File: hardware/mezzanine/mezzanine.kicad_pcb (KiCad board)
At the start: 2 copper layers, 85 x 56 mm, 43 parts, among them J1 USB_A, J2 USB_C, J3 HDMI_D, J4 HDMI_D, U1 AP22653W6, U2 TPD4EUSB30, U3 TPD4EUSB30, U4 TPD4EUSB30, U5 MagJack-A70-112-331N126, U6 RT9742SNGV, U7 74LVC1G07SE-7

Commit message: finished mezzanine signal routing
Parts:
- removed C10, C11, C12, C13, C14: 100n, Capacitor_SMD:C_0402_1005Metric
- removed the C7 at (263.2, 80.6)
- removed the C8 at (257.2, 86.8)
- removed the C9 at (248.0, 97.2)
- removed H4: MountingHole, MountingHole:MountingHole_2.7mm_M2.5
- removed TP1: TestPoint, TestPoint:TestPoint_Pad_2.0x2.0mm
- added H3: MountingHole, MountingHole:MountingHole_2.7mm_M2.5, F.Cu at (81.5, 23.5)
- C7: renamed from C15; footprint Capacitor_SMD:C_0402_1005Metric -> Capacitor_SMD:C_0603_1608Metric
- C8: renamed from C16; footprint Capacitor_SMD:C_0402_1005Metric -> Capacitor_SMD:C_0603_1608Metric
- C9: renamed from C17; footprint Capacitor_SMD:C_0402_1005Metric -> Capacitor_SMD:C_0603_1608Metric
- Module1: value cm4-module-A -> hirose-100
- Module2: value cm4-module-B -> hirose-100
- R1: footprint Resistor_SMD:R_0402_1005Metric -> Resistor_SMD:R_0805_2012Metric
- R4, R5, R6: footprint Resistor_SMD:R_0402_1005Metric -> Resistor_SMD:R_0603_1608Metric
- U2, U4: moved to B.Cu
- moved R2 200.5 mm to (40.0, 69.5), turned to -90 degrees
- moved R3 198.5 mm to (38.0, 69.5), turned to -90 degrees
- moved C1 178.4 mm to (90.5, 56.0), turned to 180 degrees
- moved C3 170.1 mm to (94.0, 59.5), turned to 90 degrees
- moved C8 166.4 mm to (39.0, 73.5)
- moved C9 166.3 mm to (39.0, 72.0), turned to 180 degrees
- moved R6 165.7 mm to (23.0, 67.0), turned to 90 degrees
- moved D2 164.6 mm to (21.0, 63.0), turned to 90 degrees
- moved U1 164.3 mm to (90.5, 59.5), turned to -90 degrees
- moved R1 163.3 mm to (90.5, 63.0)
- moved R7 162.7 mm to (23.0, 63.0), turned to 90 degrees
- moved U2 161.9 mm to (89.0, 64.0)
- moved D1 160.3 mm to (21.0, 67.0), turned to 90 degrees
- moved U7 159.9 mm to (22.0, 59.0), turned to -90 degrees
- moved C5 159.3 mm to (96.0, 59.5), turned to 90 degrees
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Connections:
- net /usb/nOCS1 renamed /usb/nUSB_CURR_FAULT
- J3 pad 1: /HDMI1_HOTPLUG -> /HDMI0_HOTPLUG
- J3 pad 11: /HDMI1_TX0_N -> /HDMI0_TX0_N
- J3 pad 12: /HDMI1_CLK_P -> /HDMI0_CLK_P
- J3 pad 14: /HDMI1_CLK_N -> /HDMI0_CLK_N
- J3 pad 15: /HDMI1_CEC -> /HDMI0_CEC
- J3 pad 17: /HDMI1_SCL -> /HDMI0_SCL
- J3 pad 18: /HDMI1_SDA -> /HDMI0_SDA
- J3 pad 3: /HDMI1_TX2_P -> /HDMI0_TX2_P
- J3 pad 5: /HDMI1_TX2_N -> /HDMI0_TX2_N
- J3 pad 6: /HDMI1_TX1_P -> /HDMI0_TX1_P
- J3 pad 8: /HDMI1_TX1_N -> /HDMI0_TX1_N
- J3 pad 9: /HDMI1_TX0_P -> /HDMI0_TX0_P
- J4 pad 1: /HDMI0_HOTPLUG -> /HDMI1_HOTPLUG
- J4 pad 11: /HDMI0_TX0_N -> /HDMI1_TX0_N
- J4 pad 12: /HDMI0_CLK_P -> /HDMI1_CLK_P
- J4 pad 14: /HDMI0_CLK_N -> /HDMI1_CLK_N
- J4 pad 15: /HDMI0_CEC -> /HDMI1_CEC
- J4 pad 17: /HDMI0_SCL -> /HDMI1_SCL
- J4 pad 18: /HDMI0_SDA -> /HDMI1_SDA
- J4 pad 3: /HDMI0_TX2_P -> /HDMI1_TX2_P
- J4 pad 5: /HDMI0_TX2_N -> /HDMI1_TX2_N
- J4 pad 6: /HDMI0_TX1_P -> /HDMI1_TX1_P
- J4 pad 8: /HDMI0_TX1_N -> /HDMI1_TX1_N
- J4 pad 9: /HDMI0_TX0_P -> /HDMI1_TX0_P
- Module1 pad 10: /TRD0_N -> /TRD3_P
- Module1 pad 100: unconnected-(Module1-Pad100) -> GND
- Module1 pad 11: /TRD2_P -> /TRD1_N
- Module1 pad 12: /TRD0_P -> /TRD3_N
- Module1 pad 15: /ETH_LEDY -> /TR1_TAP
- Module1 pad 16: unconnected-(Module1-Pad16) -> /TR3_TAP
- Module1 pad 17: /ETH_LEDG -> /TR1_TAP
- Module1 pad 18: unconnected-(Module1-Pad18) -> /TR3_TAP
- Module1 pad 19: unconnected-(Module1-Pad19) -> /TR1_TAP
- Module1 pad 20: unconnected-(Module1-Pad20) -> /TR3_TAP
- Module1 pad 21: /nPI_LED_ACTIVITY -> GND
- Module1 pad 23: GND -> /TR2_TAP
- Module1 pad 24: unconnected-(Module1-Pad24) -> /TR0_TAP
- Module1 pad 25: unconnected-(Module1-Pad25) -> /TR2_TAP
- Module1 pad 27: /TR1_TAP -> /TR2_TAP
- Module1 pad 29: /TR1_TAP -> GND
- Module1 pad 3: /TRD3_P -> /TRD0_N
- Module1 pad 30: /TR0_TAP -> GND
- Module1 pad 31: /TR1_TAP -> VBUS
- Module1 pad 32: GND -> VBUS
- Module1 pad 33: GND -> VBUS
- Module1 pad 34: unconnected-(Module1-Pad34) -> VBUS
- Module1 pad 35: unconnected-(Module1-Pad35) -> VBUS
- Module1 pad 36: /TR2_TAP -> VBUS
- Module1 pad 37: /TR3_TAP -> VBUS
- Module1 pad 38: /TR2_TAP -> VBUS
- Module1 pad 39: /TR3_TAP -> VBUS
- Module1 pad 4: /TRD1_P -> /TRD2_P
- Module1 pad 40: /TR2_TAP -> VBUS
- Module1 pad 41: /TR3_TAP -> VBUS
- Module1 pad 42: GND -> VBUS
- Module1 pad 43: GND -> VBUS
- Module1 pad 44: unconnected-(Module1-Pad44) -> VBUS
- Module1 pad 45: unconnected-(Module1-Pad45) -> GND
- Module1 pad 46: unconnected-(Module1-Pad46) -> GND
- Module1 pad 47: unconnected-(Module1-Pad47) -> GND
- Module1 pad 48: unconnected-(Module1-Pad48) -> /+3.3v
- Module1 pad 49: unconnected-(Module1-Pad49) -> /AnalogIP1
- Module1 pad 5: /TRD3_N -> /TRD0_P
- Module1 pad 50: unconnected-(Module1-Pad50) -> /+3.3v
- Module1 pad 51: unconnected-(Module1-Pad51) -> /AnalogIP0
- Module1 pad 54: unconnected-(Module1-Pad54) -> /ETH_LEDY
- Module1 pad 55: unconnected-(Module1-Pad55) -> /USB2_HOST_P
- Module1 pad 56: unconnected-(Module1-Pad56) -> /ETH_LEDG
- Module1 pad 57: unconnected-(Module1-Pad57) -> /USB2_HOST_N
- Module1 pad 58: unconnected-(Module1-Pad58) -> /nPI_LED_ACTIVITY
- Module1 pad 6: /TRD1_N -> /TRD2_N
- Module1 pad 60: GND -> /nPI_LED_PWR
- Module1 pad 61: unconnected-(Module1-Pad61) -> /USB2_DEV_N
- Module1 pad 62: unconnected-(Module1-Pad62) -> GND
- Module1 pad 63: unconnected-(Module1-Pad63) -> /USB2_DEV_P
- Module1 pad 64: unconnected-(Module1-Pad64) -> GND
- Module1 pad 67: unconnected-(Module1-Pad67) -> /HDMI1_HOTPLUG
- Module1 pad 68: unconnected-(Module1-Pad68) -> /HDMI0_HOTPLUG
- Module1 pad 69: unconnected-(Module1-Pad69) -> /HDMI1_CEC
- Module1 pad 70: unconnected-(Module1-Pad70) -> /HDMI0_CEC
- Module1 pad 71: GND -> /HDMI1_SDA
- Module1 pad 72: unconnected-(Module1-Pad72) -> /HDMI0_SDA
- Module1 pad 73: unconnected-(Module1-Pad73) -> /HDMI1_SCL
- Module1 pad 74: GND -> /HDMI0_SCL
- Module1 pad 75: unconnected-(Module1-Pad75) -> GND
- Module1 pad 76: unconnected-(Module1-Pad76) -> GND
- Module1 pad 77: VBUS -> /HDMI1_TX0_P
- Module1 pad 78: unconnected-(Module1-Pad78) -> /HDMI0_TX0_N
- Module1 pad 79: VBUS -> /HDMI1_TX0_N
- Module1 pad 80: unconnected-(Module1-Pad80) -> /HDMI0_TX0_P
- Module1 pad 81: VBUS -> GND
- Module1 pad 82: unconnected-(Module1-Pad82) -> GND
- Module1 pad 83: VBUS -> /HDMI1_TX2_P
- Module1 pad 84: /+3.3v -> /HDMI0_TX2_N
- Module1 pad 85: VBUS -> /HDMI1_TX2_N
- Module1 pad 86: /+3.3v -> /HDMI0_TX2_P
- Module1 pad 87: VBUS -> GND
- Module1 pad 88: unconnected-(Module1-Pad88) -> GND
- Module1 pad 89: unconnected-(Module1-Pad89) -> /HDMI0_TX1_P
- Module1 pad 9: /TRD2_N -> /TRD1_P
- Module1 pad 90: unconnected-(Module1-Pad90) -> /HDMI1_CLK_N
- Module1 pad 91: unconnected-(Module1-Pad91) -> /HDMI0_TX1_N
- Module1 pad 92: unconnected-(Module1-Pad92) -> /HDMI1_CLK_P
- Module1 pad 93: unconnected-(Module1-Pad93) -> GND
- Module1 pad 94: /AnalogIP1 -> GND
- Module1 pad 95: /nPI_LED_PWR -> /HDMI0_CLK_P
- Module1 pad 96: /AnalogIP0 -> /HDMI1_TX1_N
- Module1 pad 97: unconnected-(Module1-Pad97) -> /HDMI0_CLK_N
- Module1 pad 98: GND -> /HDMI1_TX1_P
- Module1 pad 99: unconnected-(Module1-Pad99) -> GND
- Module2 pad 100: /HDMI0_SCL -> unconnected-(Module2-Pad100)
- Module2 pad 13: GND -> unconnected-(Module2-Pad13)
- Module2 pad 14: GND -> unconnected-(Module2-Pad14)
- Module2 pad 19: GND -> unconnected-(Module2-Pad19)
- Module2 pad 20: GND -> unconnected-(Module2-Pad20)
- Module2 pad 25: GND -> unconnected-(Module2-Pad25)
- Module2 pad 26: GND -> unconnected-(Module2-Pad26)
- Module2 pad 3: /USB2_HOST_N -> unconnected-(Module2-Pad3)
- Module2 pad 31: GND -> unconnected-(Module2-Pad31)
- Module2 pad 32: GND -> unconnected-(Module2-Pad32)
- Module2 pad 37: GND -> unconnected-(Module2-Pad37)
- Module2 pad 38: GND -> unconnected-(Module2-Pad38)
- Module2 pad 43: /HDMI1_HOTPLUG -> unconnected-(Module2-Pad43)
- Module2 pad 44: GND -> unconnected-(Module2-Pad44)
- Module2 pad 45: /HDMI1_SDA -> unconnected-(Module2-Pad45)
- Module2 pad 46: /HDMI1_TX2_P -> unconnected-(Module2-Pad46)
- Module2 pad 47: /HDMI1_SCL -> unconnected-(Module2-Pad47)
- Module2 pad 48: /HDMI1_TX2_N -> unconnected-(Module2-Pad48)
- Module2 pad 49: /HDMI1_CEC -> unconnected-(Module2-Pad49)
- Module2 pad 5: /USB2_HOST_P -> unconnected-(Module2-Pad5)
- Module2 pad 50: GND -> unconnected-(Module2-Pad50)
- Module2 pad 51: /HDMI0_CEC -> unconnected-(Module2-Pad51)
- Module2 pad 52: /HDMI1_TX1_P -> unconnected-(Module2-Pad52)
- Module2 pad 53: /HDMI0_HOTPLUG -> unconnected-(Module2-Pad53)
- Module2 pad 54: /HDMI1_TX1_N -> unconnected-(Module2-Pad54)
- Module2 pad 55: GND -> unconnected-(Module2-Pad55)
- Module2 pad 56: GND -> unconnected-(Module2-Pad56)
- Module2 pad 58: /HDMI1_TX0_P -> unconnected-(Module2-Pad58)
- Module2 pad 60: /HDMI1_TX0_N -> unconnected-(Module2-Pad60)
- Module2 pad 61: GND -> unconnected-(Module2-Pad61)
- Module2 pad 62: GND -> unconnected-(Module2-Pad62)
- Module2 pad 64: /HDMI1_CLK_P -> unconnected-(Module2-Pad64)
- Module2 pad 66: /HDMI1_CLK_N -> unconnected-(Module2-Pad66)
- Module2 pad 67: GND -> unconnected-(Module2-Pad67)
- Module2 pad 68: GND -> unconnected-(Module2-Pad68)
- Module2 pad 7: GND -> unconnected-(Module2-Pad7)
- Module2 pad 70: /HDMI0_TX2_P -> unconnected-(Module2-Pad70)
- Module2 pad 72: /HDMI0_TX2_N -> unconnected-(Module2-Pad72)
- Module2 pad 73: GND -> unconnected-(Module2-Pad73)
- Module2 pad 74: GND -> unconnected-(Module2-Pad74)
- Module2 pad 76: /HDMI0_TX1_P -> unconnected-(Module2-Pad76)
- Module2 pad 78: /HDMI0_TX1_N -> unconnected-(Module2-Pad78)
- Module2 pad 79: GND -> unconnected-(Module2-Pad79)
- Module2 pad 8: GND -> unconnected-(Module2-Pad8)
- Module2 pad 80: GND -> unconnected-(Module2-Pad80)
- Module2 pad 82: /HDMI0_TX0_P -> unconnected-(Module2-Pad82)
- Module2 pad 84: /HDMI0_TX0_N -> unconnected-(Module2-Pad84)
- Module2 pad 85: GND -> unconnected-(Module2-Pad85)
- Module2 pad 86: GND -> unconnected-(Module2-Pad86)
- Module2 pad 88: /HDMI0_CLK_P -> unconnected-(Module2-Pad88)
- Module2 pad 90: /HDMI0_CLK_N -> unconnected-(Module2-Pad90)
- Module2 pad 91: GND -> unconnected-(Module2-Pad91)
- Module2 pad 92: GND -> unconnected-(Module2-Pad92)
- Module2 pad 93: /USB2_DEV_N -> unconnected-(Module2-Pad93)
- Module2 pad 95: /USB2_DEV_P -> unconnected-(Module2-Pad95)
- Module2 pad 97: GND -> unconnected-(Module2-Pad97)
- Module2 pad 98: GND -> unconnected-(Module2-Pad98)
- Module2 pad 99: /HDMI0_SDA -> unconnected-(Module2-Pad99)
- R2 pad 1: /AnalogIP0 -> Net-(R2-Pad1)
- R3 pad 1: /AnalogIP1 -> Net-(R3-Pad1)
- U2 pad 1: /USB2_HOST_P -> /USB2_DEV_P
- U2 pad 10: /USB2_HOST_P -> /USB2_DEV_P
- U2 pad 2: /USB2_HOST_N -> /USB2_DEV_N
- U2 pad 4: /USB2_DEV_P -> /USB2_HOST_N
- U2 pad 5: /USB2_DEV_N -> /USB2_HOST_P
- U2 pad 6: /USB2_DEV_N -> /USB2_HOST_P
- U2 pad 7: /USB2_DEV_P -> /USB2_HOST_N
- U2 pad 9: /USB2_HOST_N -> /USB2_DEV_N
- U3 pad 1: /TRD3_P -> /TRD2_P
- U3 pad 10: /TRD3_P -> /TRD2_P
- U3 pad 2: /TRD3_N -> /TRD2_N
- U3 pad 4: /TRD2_N -> /TRD3_P
- U3 pad 5: /TRD2_P -> /TRD3_N
- U3 pad 6: /TRD2_P -> /TRD3_N
- U3 pad 7: /TRD2_N -> /TRD3_P
- U3 pad 9: /TRD3_N -> /TRD2_N
- U4 pad 1: /TRD1_P -> /TRD1_N
- U4 pad 10: /TRD1_P -> /TRD1_N
- U4 pad 2: /TRD1_N -> /TRD1_P
- U4 pad 9: /TRD1_N -> /TRD1_P
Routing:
- net /nPI_LED_ACTIVITY: track 0.00 -> 255.9 mm, vias 0 -> 1
- net /nPI_LED_PWR: track 0.00 -> 192.5 mm, vias 0 -> 1
- net /USB2_DEV_N: track 0.00 -> 84.8 mm, vias 0 -> 1
- net /USB2_DEV_P: track 0.00 -> 82.1 mm, vias 0 -> 1
- net /HDMI0_TX1_P: track 0.00 -> 56.7 mm
- net /HDMI0_CLK_N: track 0.00 -> 54.9 mm
- net /HDMI0_TX1_N: track 0.00 -> 53.0 mm
- net /HDMI0_CLK_P: track 0.00 -> 51.0 mm
- net /ETH_LEDY: track 0.00 -> 49.4 mm, vias 0 -> 3
- net /ETH_LEDG: track 0.00 -> 48.3 mm, vias 0 -> 3
- net /TR1_TAP: track 0.00 -> 45.0 mm, vias 0 -> 1
- net /HDMI1_TX0_P: track 0.00 -> 44.3 mm, vias 0 -> 1
- net /HDMI1_TX0_N: track 0.00 -> 43.7 mm, vias 0 -> 1
- net /TR2_TAP: track 0.00 -> 43.4 mm, vias 0 -> 1
- net /HDMI1_TX2_P: track 0.00 -> 41.2 mm, vias 0 -> 1
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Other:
- outline, holes or cut-outs redrawn
- copper layers 2 -> 4
- board text added: "Board thickness : 1.2mm Finished copper weight inners : 0.5oz Finished copper weight outers : 1oz Board finish : OSP Material type : FR4 Colour of solder resists : Green Colour of silk screens : White Board to : UL94-V0 TG >=130 50R trace width 28.5 mil @ 2 GHz 90R diff pair width 13.5 mil spacing 3.5 mil @ 480 MHz 100R diff pair width 10 mil spacing 3.5 mil @ 2 GHz"

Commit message: move structural hirose connector
to match location on the lobby board
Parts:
- moved Module2 7.00 mm to (22.1, 40.5)
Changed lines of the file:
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@@
   )
   (footprint "cm4crypto:DF40C-100DP-0.4V(51)" (layer "B.Cu")
-    (at 22.1 47.5 180)
+    (at 22.1 40.5 180)
     (property "Field4" "Hirose")
     (property "Field5" "2x DF40C-100DS-0.4V")

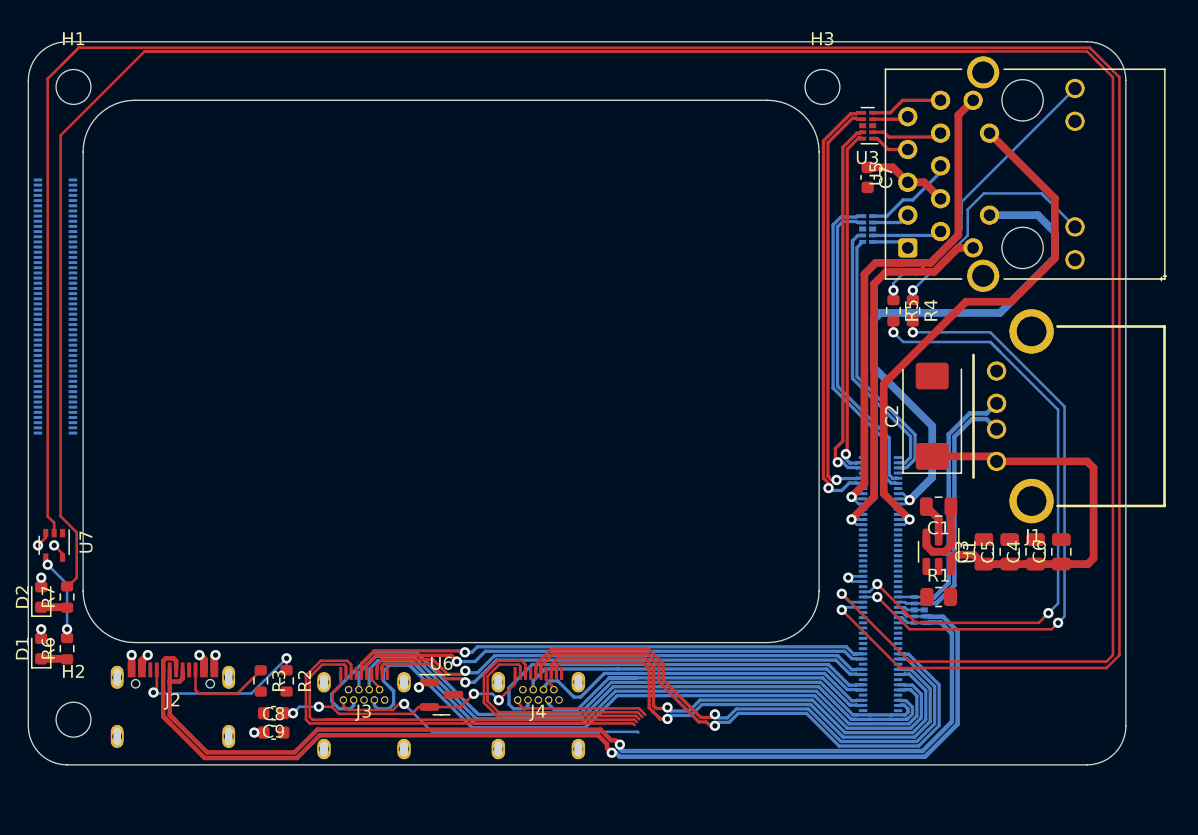
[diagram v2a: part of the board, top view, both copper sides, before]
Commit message: addtl hdmi routing
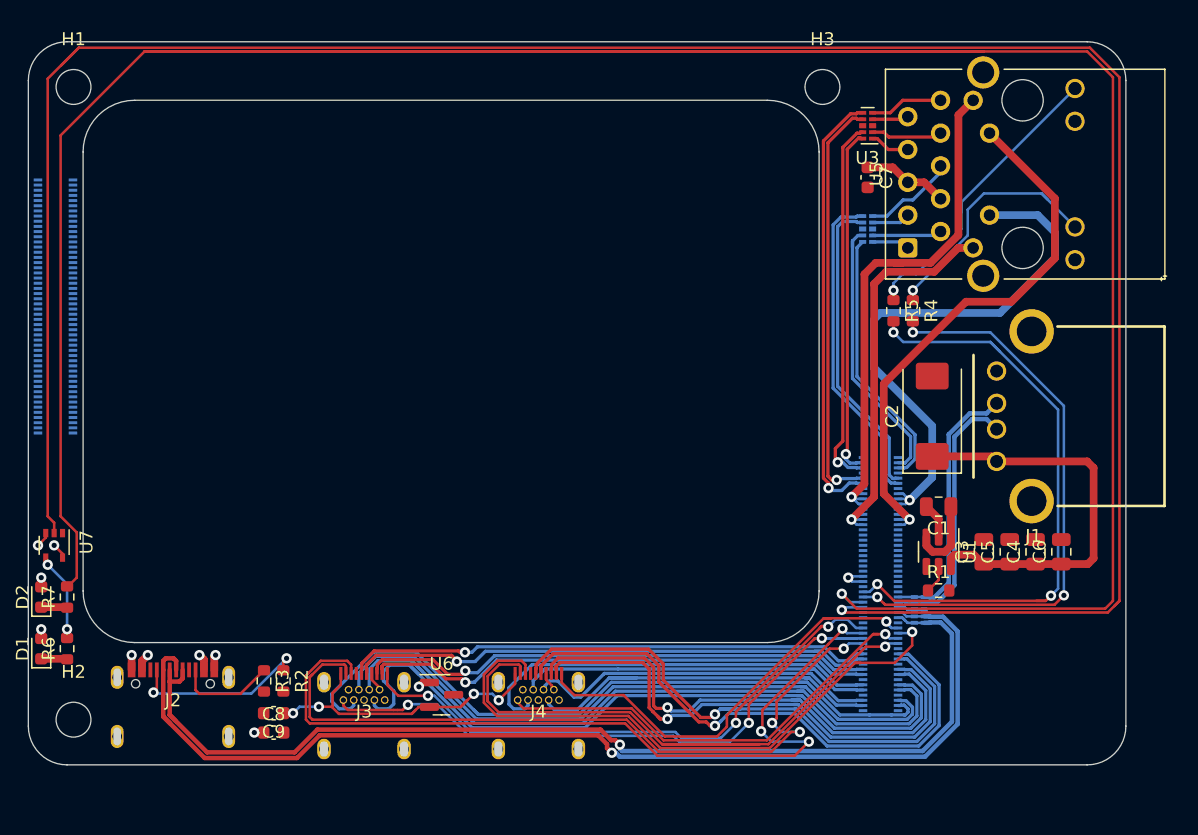
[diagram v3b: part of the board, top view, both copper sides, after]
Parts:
- R1: footprint Resistor_SMD:R_0805_2012Metric -> Resistor_SMD:R_0603_1608Metric
- moved R1 0.50 mm to (90.5, 62.5)
- moved R2 0.25 mm to (39.8, 69.5)
- moved R3 0.25 mm to (38.2, 69.5)
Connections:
- net VBUS renamed /usb/+5v
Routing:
- net /HDMI0_HOTPLUG: track 0.00 -> 44.6 mm, vias 0 -> 3
- net /HDMI1_HOTPLUG: track 0.00 -> 34.1 mm, vias 0 -> 1
- net /HDMI1_SCL: track 18.3 -> 49.8 mm, vias 0 -> 1
- net /HDMI0_CEC: track 34.1 -> 65.4 mm, vias 0 -> 3
- net /HDMI1_CEC: track 19.5 -> 47.2 mm, vias 0 -> 1
- net /HDMI1_SDA: track 10.5 -> 34.8 mm, vias 0 -> 1
- net /HDMI0_SDA: track 26.3 -> 49.2 mm, vias 1 -> 3
- net /HDMI0_SCL: track 38.2 -> 59.7 mm, vias 0 -> 3
- net /nPI_LED_ACTIVITY: track 255.9 -> 250.0 mm
- net /nPI_LED_PWR: track 192.5 -> 187.0 mm
- net /ETH_LEDG: track 48.3 -> 45.7 mm
- net Net-(R1-Pad1): track 0.00 -> 2.20 mm
- net /HDMI1_TX0_N: track 43.7 -> 45.1 mm
- net /ETH_LEDY: track 49.4 -> 48.0 mm
- net /HDMI0_TX0_P: track 40.3 -> 41.2 mm
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
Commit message: run drc on mezzanine
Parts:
- R1: value 15K 1% -> 15K
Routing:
- net /+3.3v: track 5.10 -> 184.3 mm, vias 4 -> 5
- net /usb/+5v: track 10.7 -> 50.0 mm, vias 4 -> 7
- net GND: track 11.4 -> 23.4 mm, vias 3 -> 13
- net /TRD2_P: track 30.2 -> 31.0 mm
- net /TRD2_N: track 34.4 -> 35.2 mm
- net /TRD3_P: track 35.0 -> 35.8 mm
- net /TRD3_N: track 39.7 -> 40.4 mm
- net /TRD1_P: track 26.8 -> 27.6 mm
- net /TRD1_N: track 32.1 -> 32.9 mm
- net /TRD0_P: track 23.4 -> 24.2 mm
- net /TRD0_N: track 26.6 -> 27.4 mm
- net /nPI_LED_ACTIVITY: track 250.0 -> 250.7 mm
- net /HDMI1_CEC: track 47.2 -> 47.8 mm
- added copper zone on B.Cu, net /usb/+5v
- added copper zone on In2.Cu, net /usb/+5v
- added copper zone on B.Cu, net GND
- added copper zone on F.Cu, net GND
- added copper zone on In1.Cu, net GND
- added copper zone on In2.Cu, net GND
